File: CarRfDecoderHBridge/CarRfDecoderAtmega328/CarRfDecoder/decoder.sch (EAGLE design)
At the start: 52 parts, among them T1 BC847, T2 BC847, T3 IRLML6402, U2 RFM69CW, U3 MCP73831, U4 ATMEGA328P, U6 MIC5219 3.3V, Y1 16MHZ

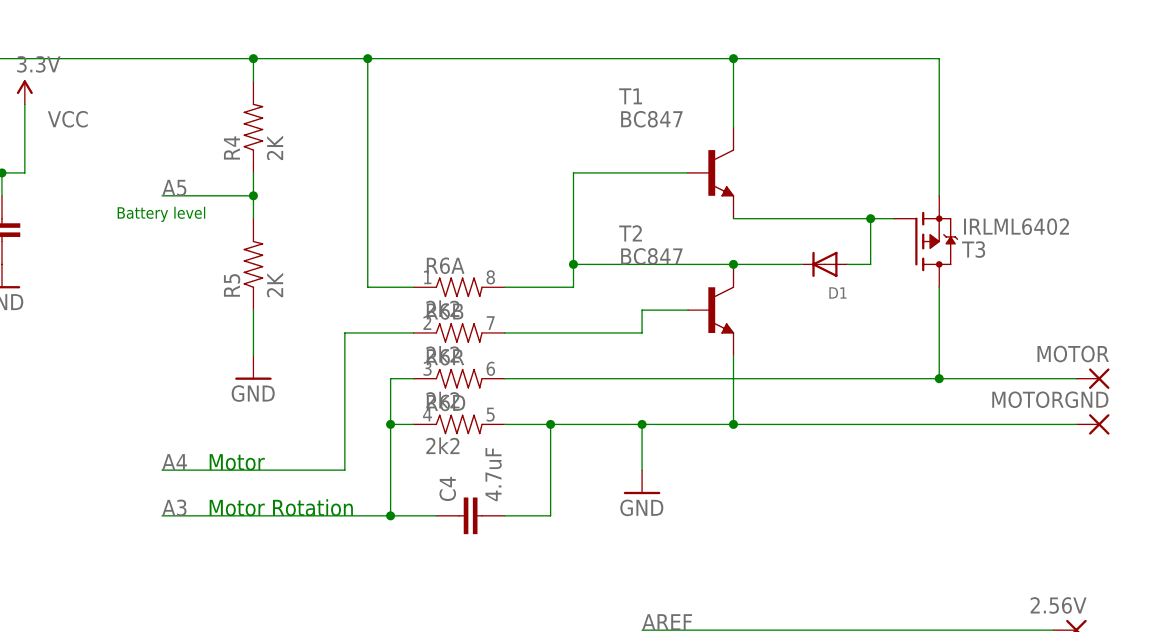
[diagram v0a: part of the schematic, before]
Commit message: Add Board with hbridge
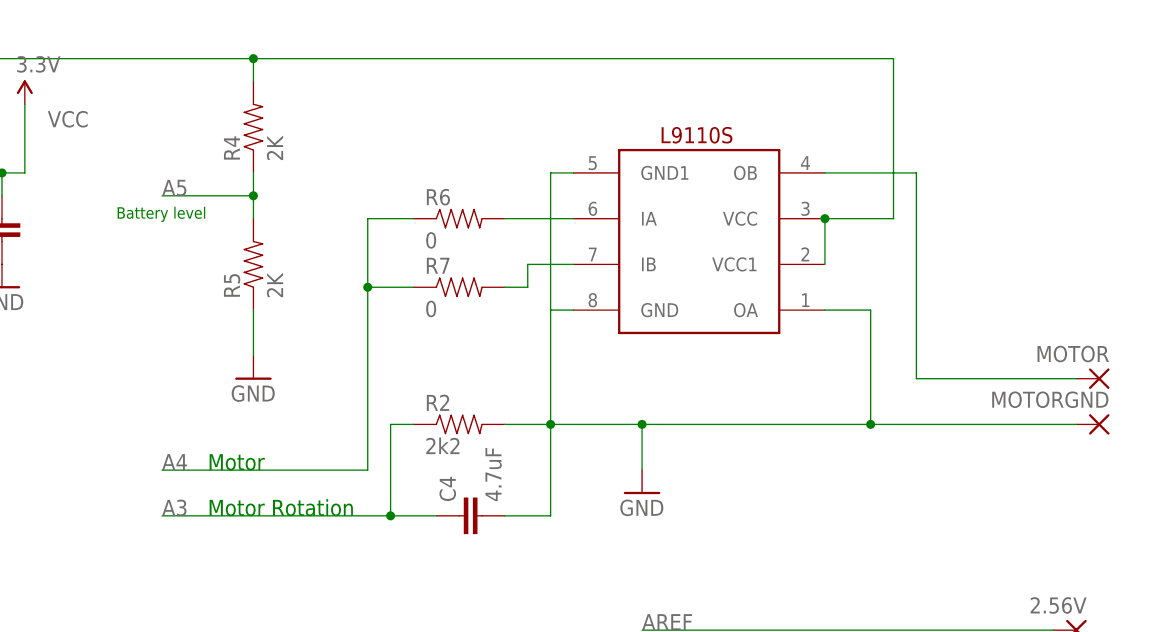
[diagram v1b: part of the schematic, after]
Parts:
- removed D1: (no value), adafruit:DIODESOD-523
- removed T1, T2: BC847, transistor:BC847
- removed T3: IRLML6402, we-transistor:MOSFET-P-SOT23
- added MDRIVER: L9110S, h-bridge-l9119s:L9110S
- added R2: 2k2, SparkFun-Resistors:RESISTOR0603-RES
- added R7: 0, SparkFun-Resistors:RESISTOR0603-RES
- R6: value 2k2 -> 0; device SparkFun-Resistors:RESISTOR-ARRAY0603-ARV -> SparkFun-Resistors:RESISTOR0603-RES
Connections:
- removed net N$14: D1.A, T1.E, T3.G
- removed net N$15: MOTOR.P, R6R.2, T3.D
- removed net N$17: R6B.2, T2.B
- removed net N$19: D1.C, R6A.2, T1.B, T2.C
- new net N$6: MDRIVER.IA, R6.2
- new net N$7: MDRIVER.IB, R7.2
- new net OB: MDRIVER.OB, MOTOR.P
- net A3: now also R2.1; no longer R6D.1, R6R.1
- net A4: now also R6.1, R7.1; no longer R6B.1
- net BAT+: now also MDRIVER.VCC, MDRIVER.VCC1; no longer R6A.1, T1.C, T3.S
- net GND: now also MDRIVER.GND, MDRIVER.GND1, MDRIVER.OA, R2.2; no longer R6D.2, T2.E

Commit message: bug fixes and better board routing
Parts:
- removed SS: (no value), wirepad:SMD2
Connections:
- removed net AX1: R9A.1, U4.PC2(ADC2)
- removed net AX2: R9B.1, U4.ADC7
- removed net AX3: R9R.1, U4.ADC6
- removed net AX4: R9D.1, U4.PD6(AIN0)
- new net A2: R9D.1, U4.PC2(ADC2)
- new net A6: C4.1, R2.1, U4.ADC6
- new net A7: R4.1, R5.2, U4.ADC7
- new net D6: R9A.1, U4.PD6(AIN0)
- net A1: now also U3.STAT; no longer R11.1
- net A3: now also R9R.1; no longer C4.1, R2.1
- net A5: now also R9B.1; no longer R4.1, R5.2
- net D7: now also R11.1; no longer U3.STAT
- net SS: no longer SS.P
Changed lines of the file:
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@@
 <part name="R1" library="SparkFun-Resistors" deviceset="RESISTOR" device="0603-RES" value="10k"/>
 <part name="VCC4" library="SparkFun-Aesthetics" deviceset="VCC" device="" value="3.3V"/>
-<part name="SS" library="wirepad" deviceset="SMD2" device=""/>
 <part name="SI" library="wirepad" deviceset="SMD2" device=""/>
 <part name="SO" library="wirepad" deviceset="SMD2" device=""/>
@@
 <instance part="R1" gate="G$1" x="15.24" y="73.66"/>
 <instance part="VCC4" gate="G$1" x="2.54" y="73.66"/>
-<instance part="SS" gate="1" x="119.38" y="27.94" rot="MR0"/>
 <instance part="SI" gate="1" x="119.38" y="22.86" rot="MR0"/>
 <instance part="SO" gate="1" x="119.38" y="17.78" rot="MR0"/>
@@
 <net name="A1" class="0">
 <segment>
-<pinref part="R11" gate="G$1" pin="1"/>
-<wire x1="185.42" y1="50.8" x2="170.18" y2="50.8" width="0.1524" layer="91"/>
-<label x="172.72" y="50.8" size="1.778" layer="95"/>
-</segment>
-<segment>
 <pinref part="U4" gate="G$1" pin="PC1(ADC1)"/>
 <wire x1="78.74" y1="71.12" x2="88.9" y2="71.12" width="0.1524" layer="91"/>
 <label x="83.82" y="71.12" size="1.778" layer="95"/>
 </segment>
+<segment>
+<pinref part="U3" gate="G$1" pin="STAT"/>
+<wire x1="15.24" y1="111.76" x2="7.62" y2="111.76" width="0.1524" layer="91"/>
+<label x="7.62" y="111.76" size="1.778" layer="95"/>
+</segment>
 </net>
 <net name="A3" class="0">
-<segment>
-<wire x1="144.78" y1="91.44" x2="147.32" y2="91.44" width="0.1524" layer="91"/>
-<wire x1="144.78" y1="91.44" x2="144.78" y2="81.28" width="0.1524" layer="91"/>
-<wire x1="144.78" y1="81.28" x2="119.38" y2="81.28" width="0.1524" layer="91"/>
-<pinref part="C4" gate="G$1" pin="1"/>
-<wire x1="144.78" y1="81.28" x2="149.86" y2="81.28" width="0.1524" layer="91"/>
-<junction x="144.78" y="81.28"/>
-<label x="119.38" y="81.28" size="1.778" layer="95"/>
-<pinref part="R2" gate="G$1" pin="1"/>
-</segment>
 <segment>
 <pinref part="U4" gate="G$1" pin="PC3(ADC3)"/>
 <wire x1="78.74" y1="66.04" x2="88.9" y2="66.04" width="0.1524" layer="91"/>
 <label x="83.82" y="66.04" size="1.778" layer="95"/>
+</segment>
+<segment>
+<pinref part="R9" gate="R" pin="1"/>
+<wire x1="185.42" y1="-12.7" x2="167.64" y2="-12.7" width="0.1524" layer="91"/>
+<label x="172.72" y="-12.7" size="1.778" layer="95"/>
 </segment>
 </net>
@@
 <net name="A5" class="0">
 <segment>
-<pinref part="R4" gate="G$1" pin="1"/>
-<pinref part="R5" gate="G$1" pin="2"/>
-<wire x1="129.54" y1="119.38" x2="129.54" y2="116.84" width="0.1524" layer="91"/>
-<wire x1="129.54" y1="116.84" x2="129.54" y2="114.3" width="0.1524" layer="91"/>
-<wire x1="129.54" y1="116.84" x2="119.38" y2="116.84" width="0.1524" layer="91"/>
-<junction x="129.54" y="116.84"/>
-<label x="119.38" y="116.84" size="1.778" layer="95"/>
-</segment>
-<segment>
 <pinref part="U4" gate="G$1" pin="PC5(ADC5/SCL)"/>
 <wire x1="78.74" y1="60.96" x2="88.9" y2="60.96" width="0.1524" layer="91"/>
 <label x="83.82" y="60.96" size="1.778" layer="95"/>
 </segment>
+<segment>
+<pinref part="R9" gate="B" pin="1"/>
+<wire x1="185.42" y1="-5.08" x2="167.64" y2="-5.08" width="0.1524" layer="91"/>
+<label x="172.72" y="-5.08" size="1.778" layer="95"/>
+</segment>
 </net>
 <net name="D7" class="0">
-<segment>
-<pinref part="U3" gate="G$1" pin="STAT"/>
-<wire x1="15.24" y1="111.76" x2="7.62" y2="111.76" width="0.1524" layer="91"/>
-<label x="7.62" y="111.76" size="1.778" layer="95"/>
-</segment>
 <segment>
 <pinref part="U4" gate="G$1" pin="PD7(AIN1)"/>
@@
 <label x="86.36" y="33.02" size="1.778" layer="95"/>
 </segment>
+<segment>
+<pinref part="R11" gate="G$1" pin="1"/>
+<wire x1="185.42" y1="50.8" x2="170.18" y2="50.8" width="0.1524" layer="91"/>
+<label x="172.72" y="50.8" size="1.778" layer="95"/>
+</segment>
 </net>
 <net name="SS" class="0">
@@
 <label x="83.82" y="22.86" size="1.778" layer="95"/>
 <wire x1="78.74" y1="22.86" x2="99.06" y2="22.86" width="0.1524" layer="91"/>
-<wire x1="99.06" y1="22.86" x2="99.06" y2="27.94" width="0.1524" layer="91"/>
-<pinref part="SS" gate="1" pin="P"/>
-<wire x1="99.06" y1="27.94" x2="116.84" y2="27.94" width="0.1524" layer="91"/>
 </segment>
 </net>
@@
 </segment>
 </net>
-<net name="AX1" class="0">
+<net name="D6" class="0">
 <segment>
 <pinref part="R9" gate="A" pin="1"/>
 <wire x1="185.42" y1="2.54" x2="167.64" y2="2.54" width="0.1524" layer="91"/>
 <label x="172.72" y="2.54" size="1.778" layer="95"/>
-</segment>
-<segment>
-<pinref part="U4" gate="G$1" pin="PC2(ADC2)"/>
-<wire x1="78.74" y1="68.58" x2="88.9" y2="68.58" width="0.1524" layer="91"/>
-<label x="83.82" y="68.58" size="1.778" layer="95"/>
-</segment>
-</net>
-<net name="AX2" class="0">
-<segment>
-<pinref part="R9" gate="B" pin="1"/>
-<wire x1="185.42" y1="-5.08" x2="167.64" y2="-5.08" width="0.1524" layer="91"/>
-<label x="172.72" y="-5.08" size="1.778" layer="95"/>
-</segment>
-<segment>
-<pinref part="U4" gate="G$1" pin="ADC7"/>
-<wire x1="78.74" y1="55.88" x2="88.9" y2="55.88" width="0.1524" layer="91"/>
-<label x="83.82" y="55.88" size="1.778" layer="95"/>
-</segment>
-</net>
-<net name="AX3" class="0">
-<segment>
-<pinref part="R9" gate="R" pin="1"/>
-<wire x1="185.42" y1="-12.7" x2="167.64" y2="-12.7" width="0.1524" layer="91"/>
-<label x="172.72" y="-12.7" size="1.778" layer="95"/>
-</segment>
-<segment>
-<pinref part="U4" gate="G$1" pin="ADC6"/>
-<wire x1="78.74" y1="58.42" x2="88.9" y2="58.42" width="0.1524" layer="91"/>
-<label x="83.82" y="58.42" size="1.778" layer="95"/>
-</segment>
-</net>
-<net name="AX4" class="0">
-<segment>
-<pinref part="R9" gate="D" pin="1"/>
-<wire x1="185.42" y1="-20.32" x2="167.64" y2="-20.32" width="0.1524" layer="91"/>
-<label x="172.72" y="-20.32" size="1.778" layer="95"/>
 </segment>
 <segment>
@@
 </segment>
 </net>
+<net name="A6" class="0">
+<segment>
+<pinref part="U4" gate="G$1" pin="ADC6"/>
+<wire x1="78.74" y1="58.42" x2="88.9" y2="58.42" width="0.1524" layer="91"/>
+<label x="83.82" y="58.42" size="1.778" layer="95"/>
+</segment>
+<segment>
+<wire x1="144.78" y1="91.44" x2="147.32" y2="91.44" width="0.1524" layer="91"/>
+<wire x1="144.78" y1="91.44" x2="144.78" y2="81.28" width="0.1524" layer="91"/>
+<wire x1="144.78" y1="81.28" x2="119.38" y2="81.28" width="0.1524" layer="91"/>
+<pinref part="C4" gate="G$1" pin="1"/>
+<wire x1="144.78" y1="81.28" x2="149.86" y2="81.28" width="0.1524" layer="91"/>
+<junction x="144.78" y="81.28"/>
+<label x="119.38" y="81.28" size="1.778" layer="95"/>
+<pinref part="R2" gate="G$1" pin="1"/>
+</segment>
+</net>
+<net name="A7" class="0">
+<segment>
+<pinref part="U4" gate="G$1" pin="ADC7"/>
+<wire x1="78.74" y1="55.88" x2="88.9" y2="55.88" width="0.1524" layer="91"/>
+<label x="83.82" y="55.88" size="1.778" layer="95"/>
+</segment>
+<segment>
+<pinref part="R4" gate="G$1" pin="1"/>
+<pinref part="R5" gate="G$1" pin="2"/>
+<wire x1="129.54" y1="119.38" x2="129.54" y2="116.84" width="0.1524" layer="91"/>
+<wire x1="129.54" y1="116.84" x2="129.54" y2="114.3" width="0.1524" layer="91"/>
+<wire x1="129.54" y1="116.84" x2="119.38" y2="116.84" width="0.1524" layer="91"/>
+<junction x="129.54" y="116.84"/>
+<label x="119.38" y="116.84" size="1.778" layer="95"/>
+</segment>
+</net>
+<net name="A2" class="0">
+<segment>
+<pinref part="U4" gate="G$1" pin="PC2(ADC2)"/>
+<wire x1="78.74" y1="68.58" x2="88.9" y2="68.58" width="0.1524" layer="91"/>
+<label x="83.82" y="68.58" size="1.778" layer="95"/>
+</segment>
+<segment>
+<pinref part="R9" gate="D" pin="1"/>
+<wire x1="185.42" y1="-20.32" x2="167.64" y2="-20.32" width="0.1524" layer="91"/>
+<label x="172.72" y="-20.32" size="1.778" layer="95"/>
+</segment>
+</net>

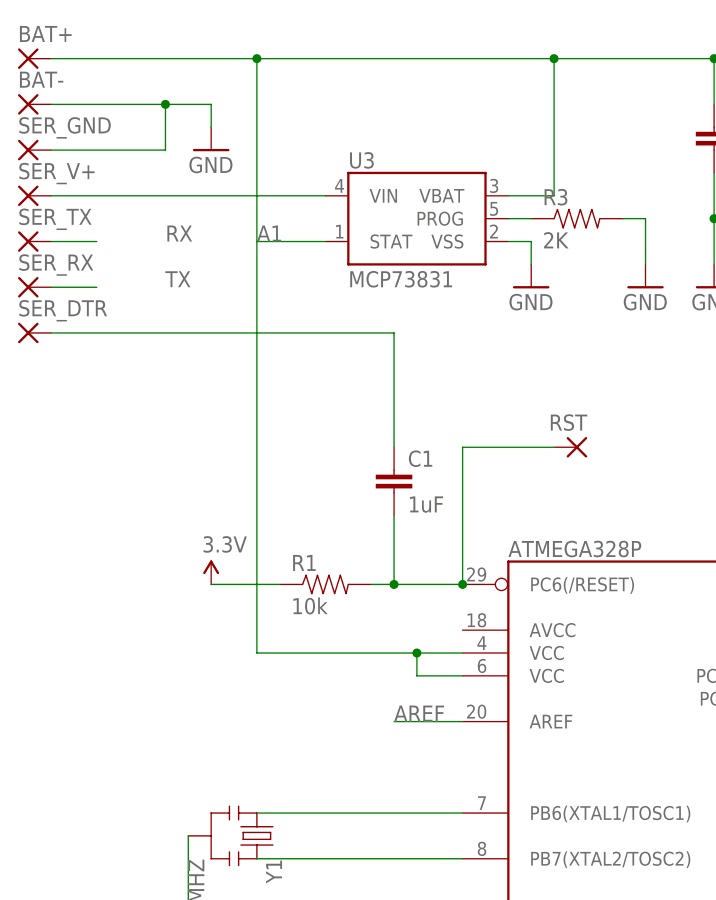
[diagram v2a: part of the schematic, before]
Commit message: Add possibility to power the board from 3.3v or direct from battery.
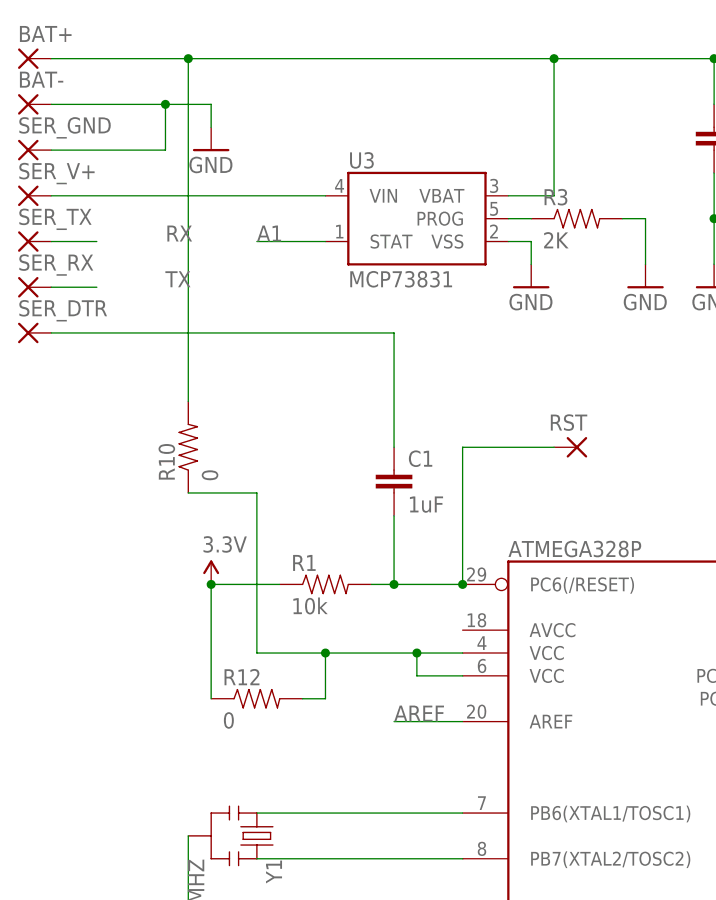
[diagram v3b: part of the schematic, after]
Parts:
- added R10, R12: 0, SparkFun-Resistors:RESISTOR0603-RES
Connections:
- new net N$8: R10.1, R12.2, U4.VCC@1, U4.VCC@2
- net BAT+: now also R10.2; no longer U4.VCC@1, U4.VCC@2
- net VCC: now also R12.1
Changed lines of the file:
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@@
 <part name="R6" library="SparkFun-Resistors" deviceset="RESISTOR" device="0603-RES" value="0"/>
 <part name="R7" library="SparkFun-Resistors" deviceset="RESISTOR" device="0603-RES" value="0"/>
+<part name="R10" library="SparkFun-Resistors" deviceset="RESISTOR" device="0603-RES" value="0"/>
+<part name="R12" library="SparkFun-Resistors" deviceset="RESISTOR" device="0603-RES" value="0"/>
 </parts>
 <sheets>
@@
 <instance part="R6" gate="G$1" x="152.4" y="114.3"/>
 <instance part="R7" gate="G$1" x="152.4" y="106.68"/>
+<instance part="R10" gate="G$1" x="0" y="88.9" rot="R90"/>
+<instance part="R12" gate="G$1" x="7.62" y="60.96"/>
 </instances>
 <busses>
@@
 <wire x1="10.16" y1="73.66" x2="2.54" y2="73.66" width="0.1524" layer="91"/>
 <pinref part="VCC4" gate="G$1" pin="VCC"/>
+<pinref part="R12" gate="G$1" pin="1"/>
+<wire x1="2.54" y1="60.96" x2="2.54" y2="73.66" width="0.1524" layer="91"/>
+<junction x="2.54" y="73.66"/>
 </segment>
 </net>
@@
 <net name="BAT+" class="0">
 <segment>
-<pinref part="U4" gate="G$1" pin="VCC@1"/>
-<wire x1="30.48" y1="66.04" x2="25.4" y2="66.04" width="0.1524" layer="91"/>
-<wire x1="25.4" y1="66.04" x2="25.4" y2="63.5" width="0.1524" layer="91"/>
-<pinref part="U4" gate="G$1" pin="VCC@2"/>
-<wire x1="25.4" y1="63.5" x2="30.48" y2="63.5" width="0.1524" layer="91"/>
 <pinref part="U6" gate="G$1" pin="EN"/>
 <wire x1="71.12" y1="109.22" x2="66.04" y2="109.22" width="0.1524" layer="91"/>
@@
 <wire x1="66.04" y1="119.38" x2="71.12" y2="119.38" width="0.1524" layer="91"/>
 <pinref part="BAT+" gate="1" pin="P"/>
-<wire x1="-15.24" y1="132.08" x2="7.62" y2="132.08" width="0.1524" layer="91"/>
 <junction x="40.64" y="132.08"/>
-<wire x1="7.62" y1="132.08" x2="40.64" y2="132.08" width="0.1524" layer="91"/>
+<wire x1="-15.24" y1="132.08" x2="0" y2="132.08" width="0.1524" layer="91"/>
+<wire x1="0" y1="132.08" x2="40.64" y2="132.08" width="0.1524" layer="91"/>
 <wire x1="40.64" y1="132.08" x2="58.42" y2="132.08" width="0.1524" layer="91"/>
 <wire x1="58.42" y1="132.08" x2="66.04" y2="132.08" width="0.1524" layer="91"/>
@@
 <pinref part="R4" gate="G$1" pin="2"/>
 <wire x1="129.54" y1="132.08" x2="129.54" y2="129.54" width="0.1524" layer="91"/>
-<wire x1="7.62" y1="132.08" x2="7.62" y2="66.04" width="0.1524" layer="91"/>
-<junction x="7.62" y="132.08"/>
-<wire x1="7.62" y1="66.04" x2="25.4" y2="66.04" width="0.1524" layer="91"/>
-<junction x="25.4" y="66.04"/>
 <junction x="129.54" y="132.08"/>
 <pinref part="MDRIVER" gate="G$1" pin="VCC1"/>
@@
 <junction x="193.04" y="114.3"/>
 <wire x1="200.66" y1="132.08" x2="129.54" y2="132.08" width="0.1524" layer="91"/>
+<pinref part="R10" gate="G$1" pin="2"/>
+<wire x1="0" y1="93.98" x2="0" y2="132.08" width="0.1524" layer="91"/>
+<junction x="0" y="132.08"/>
 </segment>
 </net>
@@
 </segment>
 </net>
+<net name="N$8" class="0">
+<segment>
+<pinref part="U4" gate="G$1" pin="VCC@2"/>
+<wire x1="25.4" y1="63.5" x2="30.48" y2="63.5" width="0.1524" layer="91"/>
+<pinref part="U4" gate="G$1" pin="VCC@1"/>
+<wire x1="30.48" y1="66.04" x2="25.4" y2="66.04" width="0.1524" layer="91"/>
+<wire x1="25.4" y1="66.04" x2="25.4" y2="63.5" width="0.1524" layer="91"/>
+<junction x="25.4" y="66.04"/>
+<wire x1="25.4" y1="66.04" x2="15.24" y2="66.04" width="0.1524" layer="91"/>
+<wire x1="15.24" y1="66.04" x2="7.62" y2="66.04" width="0.1524" layer="91"/>
+<junction x="15.24" y="66.04"/>
+<wire x1="15.24" y1="60.96" x2="15.24" y2="66.04" width="0.1524" layer="91"/>
+<pinref part="R12" gate="G$1" pin="2"/>
+<wire x1="12.7" y1="60.96" x2="15.24" y2="60.96" width="0.1524" layer="91"/>
+<wire x1="7.62" y1="66.04" x2="7.62" y2="83.82" width="0.1524" layer="91"/>
+<pinref part="R10" gate="G$1" pin="1"/>
+<wire x1="7.62" y1="83.82" x2="0" y2="83.82" width="0.1524" layer="91"/>
+</segment>
+</net>

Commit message: Better design of board
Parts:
- added BAT+1: (no value), wirepad:SMD2
- added R13: 10k, SparkFun-Resistors:RESISTOR0603-RES
- C1: value 1uF -> 0.1uF
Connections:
- net BAT+: now also BAT+1.P
- net MISO: now also R13.2
- net N$1: now also R13.1
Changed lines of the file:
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@@
 <part name="GND" library="wirepad" deviceset="SMD2" device=""/>
 <part name="GND1" library="wirepad" deviceset="SMD2" device=""/>
-<part name="C1" library="SparkFun-Capacitors" deviceset="CAP" device="0805" value="1uF"/>
+<part name="C1" library="SparkFun-Capacitors" deviceset="CAP" device="0805" value="0.1uF"/>
 <part name="RST" library="wirepad" deviceset="SMD2" device=""/>
 <part name="MDRIVER" library="h-bridge-l9119s" deviceset="L9110S" device=""/>
@@
 <part name="R10" library="SparkFun-Resistors" deviceset="RESISTOR" device="0603-RES" value="0"/>
 <part name="R12" library="SparkFun-Resistors" deviceset="RESISTOR" device="0603-RES" value="0"/>
+<part name="R13" library="SparkFun-Resistors" deviceset="RESISTOR" device="0603-RES" value="10k"/>
+<part name="BAT+1" library="wirepad" deviceset="SMD2" device=""/>
 </parts>
 <sheets>
@@
 <instance part="R10" gate="G$1" x="0" y="88.9" rot="R90"/>
 <instance part="R12" gate="G$1" x="7.62" y="60.96"/>
+<instance part="R13" gate="G$1" x="10.16" y="-20.32"/>
+<instance part="BAT+1" gate="1" x="-17.78" y="137.16"/>
 </instances>
 <busses>
@@
 <segment>
 <pinref part="U2" gate="G$1" pin="MISO"/>
-<wire x1="35.56" y1="-20.32" x2="25.4" y2="-20.32" width="0.1524" layer="91"/>
 <label x="25.4" y="-20.32" size="1.778" layer="95"/>
+<pinref part="R13" gate="G$1" pin="2"/>
+<wire x1="15.24" y1="-20.32" x2="35.56" y2="-20.32" width="0.1524" layer="91"/>
 </segment>
 <segment>
@@
 <pinref part="VJ" gate="1" pin="P"/>
 <wire x1="35.56" y1="-15.24" x2="30.48" y2="-12.7" width="0.1524" layer="91"/>
+<pinref part="R13" gate="G$1" pin="1"/>
+<wire x1="5.08" y1="-20.32" x2="5.08" y2="-15.24" width="0.1524" layer="91"/>
+<wire x1="5.08" y1="-15.24" x2="35.56" y2="-15.24" width="0.1524" layer="91"/>
+<junction x="35.56" y="-15.24"/>
 </segment>
 </net>
@@
 <wire x1="0" y1="93.98" x2="0" y2="132.08" width="0.1524" layer="91"/>
 <junction x="0" y="132.08"/>
-</segment>
-</net>
+<pinref part="BAT+1" gate="1" pin="P"/>
+<wire x1="-15.24" y1="137.16" x2="0" y2="137.16" width="0.1524" layer="91"/>
+<wire x1="0" y1="137.16" x2="0" y2="132.08" width="0.1524" layer="91"/>
+</segment>
+</net>
